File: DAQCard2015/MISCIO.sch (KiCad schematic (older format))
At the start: 3 parts

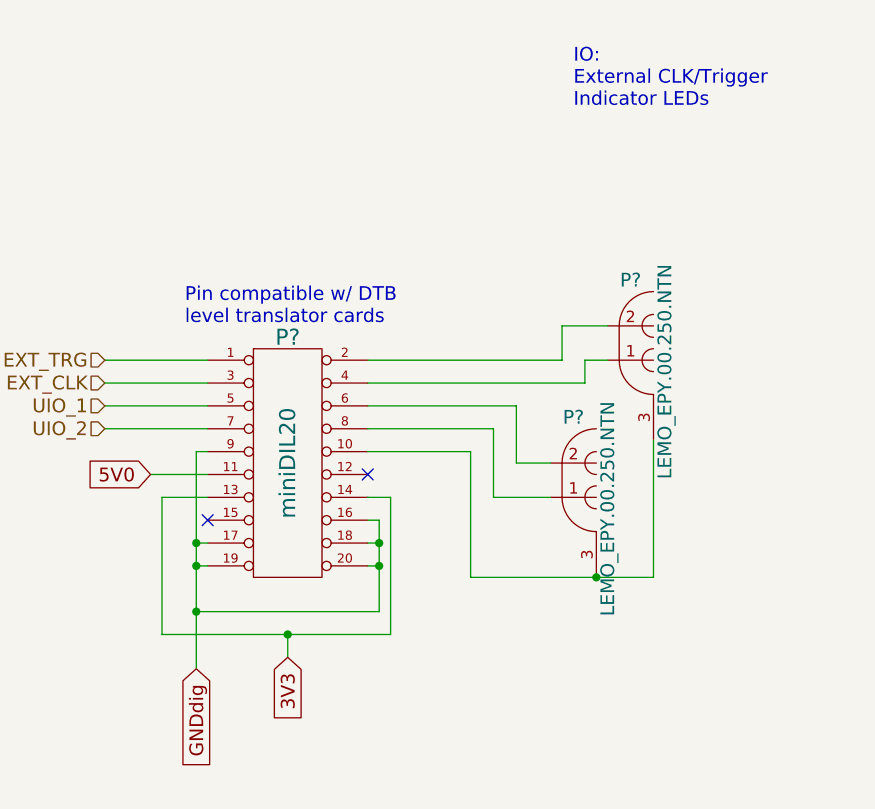
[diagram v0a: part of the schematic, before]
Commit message: Adds power circuitry to DAQCard2015
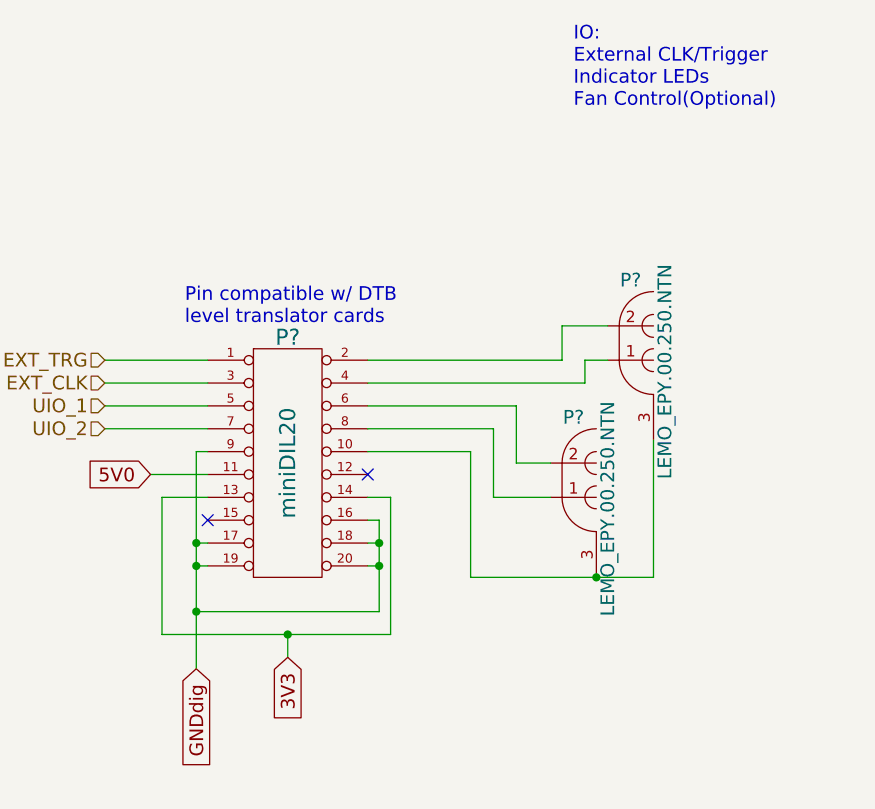
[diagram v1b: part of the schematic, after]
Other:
- note added: "IO:\nExternal CLK/Trigger\nIndicator LEDs\nFan Control(Optional)"
- note removed: "IO:\nExternal CLK/Trigger\nIndicator LEDs"
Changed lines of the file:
@@
 $EndDescr
 Text Notes 9050 900  0    60   ~ 0
-IO:\nExternal CLK/Trigger\nIndicator LEDs
+IO:\nExternal CLK/Trigger\nIndicator LEDs\nFan Control(Optional)
 $Comp
 L LEMO_EPY.00.250.NTN P?
@@
 $EndComp
 Wire Wire Line
-	7400 2400 7400 2800
-Wire Wire Line
-	7400 2800 7400 2900
-Wire Wire Line
-	7400 2900 7400 3100
-Wire Wire Line
-	7400 3100 7400 3350
+	7400 2400 7400 3350
 Wire Wire Line
 	8150 2700 8200 2700
 Wire Wire Line
-	8200 2700 8200 2800
-Wire Wire Line
-	8200 2800 8200 2900
-Wire Wire Line
-	8200 2900 8200 3100
+	8200 2700 8200 3100
 Wire Wire Line
 	8200 3100 7400 3100
@@
 	8150 2600 8250 2600
 Wire Wire Line
-	8250 2600 8250 3200
+	8250 3200 8250 2600
 Wire Wire Line
-	8250 3200 7800 3200
-Wire Wire Line
-	7800 3200 7250 3200
+	7250 3200 8250 3200
 Wire Wire Line
 	7250 3200 7250 2600
@@
 	8600 2400 8600 2950
 Wire Wire Line
-	8600 2950 9150 2950
-Wire Wire Line
-	9150 2950 9400 2950
+	8600 2950 9400 2950
 Wire Wire Line
 	9400 2950 9400 2350

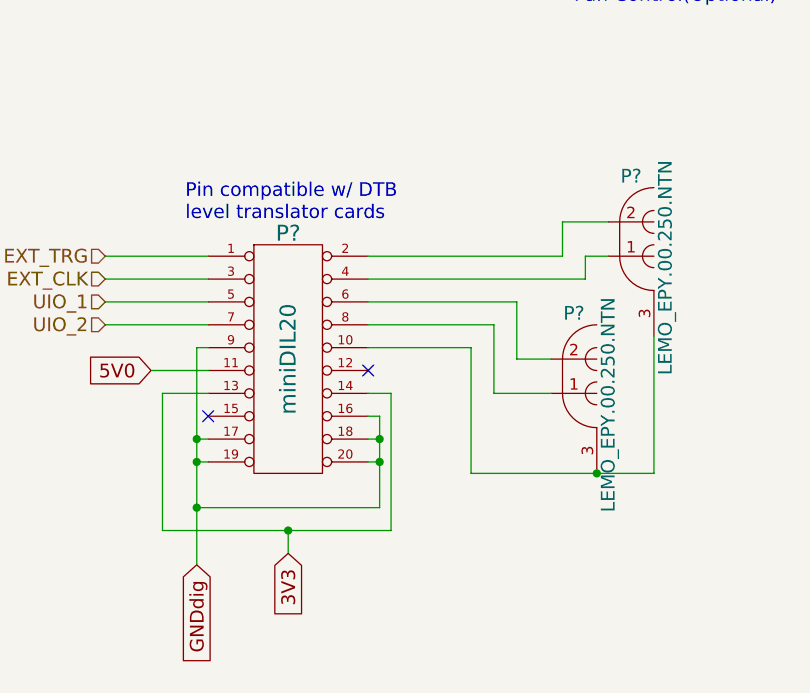
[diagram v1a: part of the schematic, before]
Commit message: Replaces single ample with 4-channel varients. Greatly reducing part count
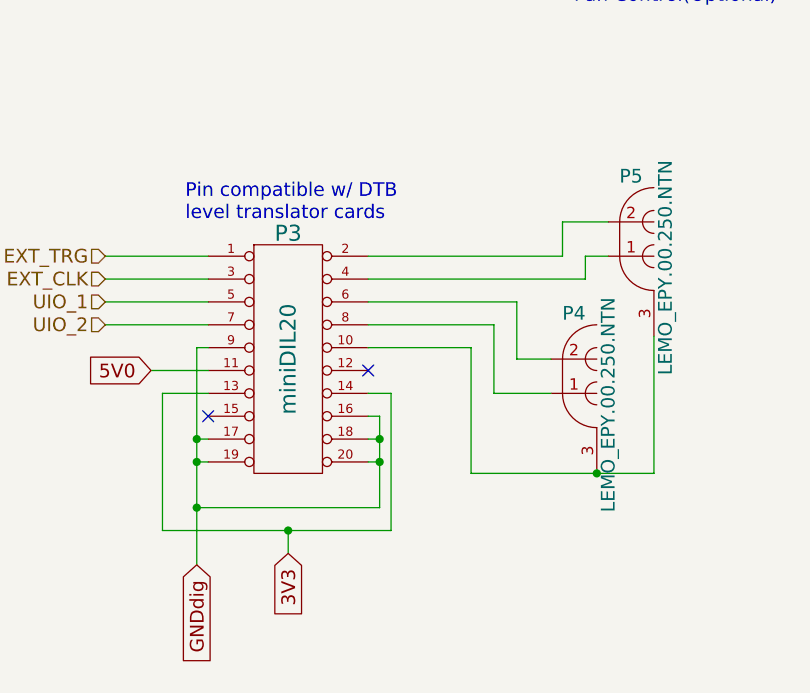
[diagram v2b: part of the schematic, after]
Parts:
- gave numbers to parts that had none: 3
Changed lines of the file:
@@
 IO:\nExternal CLK/Trigger\nIndicator LEDs\nFan Control(Optional)
 $Comp
-L LEMO_EPY.00.250.NTN P?
+L LEMO_EPY.00.250.NTN P5
 U 1 1 55D34F59
 P 9400 2000
-F 0 "P?" H 9300 2350 60  0000 C CNN
+F 0 "P5" H 9300 2350 60  0000 C CNN
 F 1 "LEMO_EPY.00.250.NTN" V 9450 1950 60  0000 C CNN
 F 2 "" H 9400 2000 60  0000 C CNN
@@
 $EndComp
 $Comp
-L LEMO_EPY.00.250.NTN P?
+L LEMO_EPY.00.250.NTN P4
 U 1 1 55D35009
 P 9150 2600
-F 0 "P?" H 9050 2950 60  0000 C CNN
+F 0 "P4" H 9050 2950 60  0000 C CNN
 F 1 "LEMO_EPY.00.250.NTN" V 9200 2550 60  0000 C CNN
 F 2 "" H 9150 2600 60  0000 C CNN
@@
 	8700 2300 8150 2300
 $Comp
-L miniDIL20 P?
+L miniDIL20 P3
 U 1 1 55D35BC1
 P 7800 2450
-F 0 "P?" H 7800 3000 70  0000 C CNN
+F 0 "P3" H 7800 3000 70  0000 C CNN
 F 1 "miniDIL20" V 7800 2450 70  0000 C CNN
 F 2 "" H 7800 2450 60  0000 C CNN
@@
 	8150 2600 8250 2600
 Wire Wire Line
-	8250 3200 8250 2600
+	8250 2600 8250 3200
 Wire Wire Line
-	7250 3200 8250 3200
+	8250 3200 7250 3200
 Wire Wire Line
 	7250 3200 7250 2600

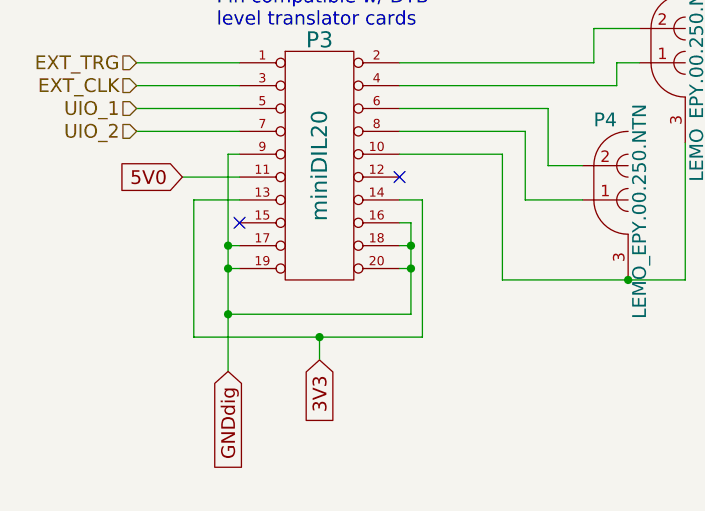
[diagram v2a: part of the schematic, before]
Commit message: Finishes initial version of schematic(mostly). And adds a whole bunch of new footprints!
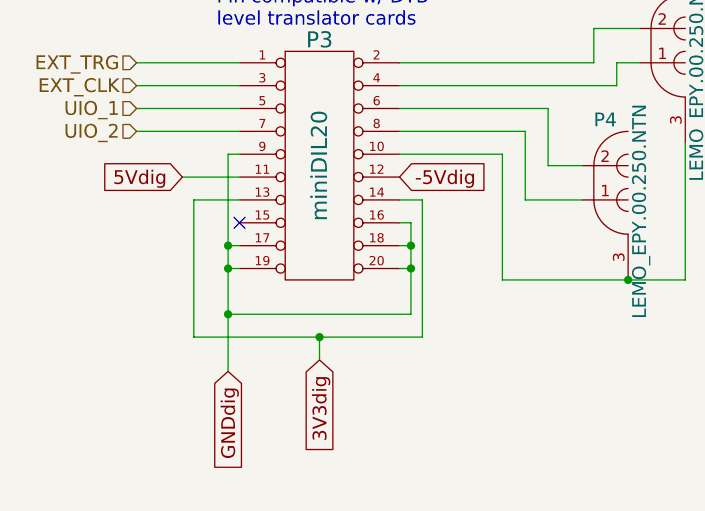
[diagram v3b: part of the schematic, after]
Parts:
- P3: footprint (none) -> extras:M50-3101045
- P4, P5: footprint (none) -> extras:EPY.00.250.NTN
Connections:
- net -5Vdig: now reaches P3.12
- net 3V3 renamed 3V3dig
- net 5V0 renamed 5Vdig
- no-connect marks 2 -> 1
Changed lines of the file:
@@
 F 0 "P5" H 9300 2350 60  0000 C CNN
 F 1 "LEMO_EPY.00.250.NTN" V 9450 1950 60  0000 C CNN
-F 2 "" H 9400 2000 60  0000 C CNN
+F 2 "extras:EPY.00.250.NTN" H 9400 2000 60  0001 C CNN
 F 3 "" H 9400 2000 60  0000 C CNN
 	1    9400 2000
@@
 F 0 "P4" H 9050 2950 60  0000 C CNN
 F 1 "LEMO_EPY.00.250.NTN" V 9200 2550 60  0000 C CNN
-F 2 "" H 9150 2600 60  0000 C CNN
+F 2 "extras:EPY.00.250.NTN" H 9150 2600 60  0001 C CNN
 F 3 "" H 9150 2600 60  0000 C CNN
 	1    9150 2600
@@
 	7400 2800 7450 2800
 NoConn ~ 7450 2700
-NoConn ~ 8150 2500
 Wire Wire Line
 	9200 1850 9000 1850
@@
 F 0 "P3" H 7800 3000 70  0000 C CNN
 F 1 "miniDIL20" V 7800 2450 70  0000 C CNN
-F 2 "" H 7800 2450 60  0000 C CNN
+F 2 "extras:M50-3101045" H 7800 2450 60  0001 C CNN
 F 3 "" H 7800 2450 60  0000 C CNN
 	1    7800 2450
@@
 $EndComp
 Text GLabel 7800 3300 3    60   Input ~ 0
-3V3
+3V3dig
 Wire Wire Line
 	8150 2600 8250 2600
@@
 	7250 2600 7450 2600
 Text GLabel 7200 2500 0    60   Input ~ 0
-5V0
+5Vdig
 Wire Wire Line
 	7450 2500 7200 2500
@@
 Text HLabel 7000 2300 0    60   Input ~ 0
 UIO_2
+Text GLabel 8150 2500 2    60   Input ~ 0
+-5Vdig
 $EndSCHEMATC

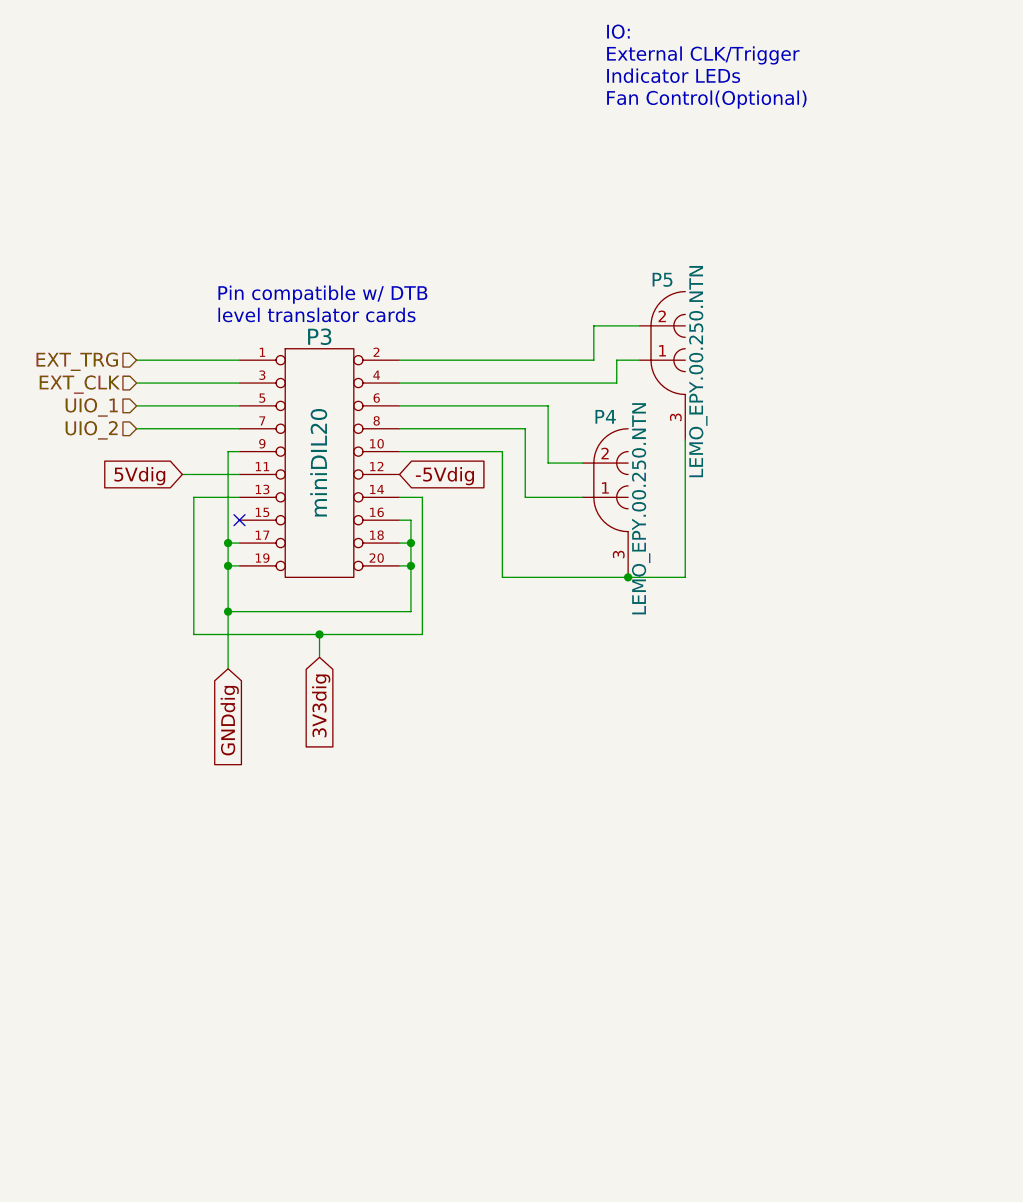
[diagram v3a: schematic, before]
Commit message: ADC channels wired, fan controller added
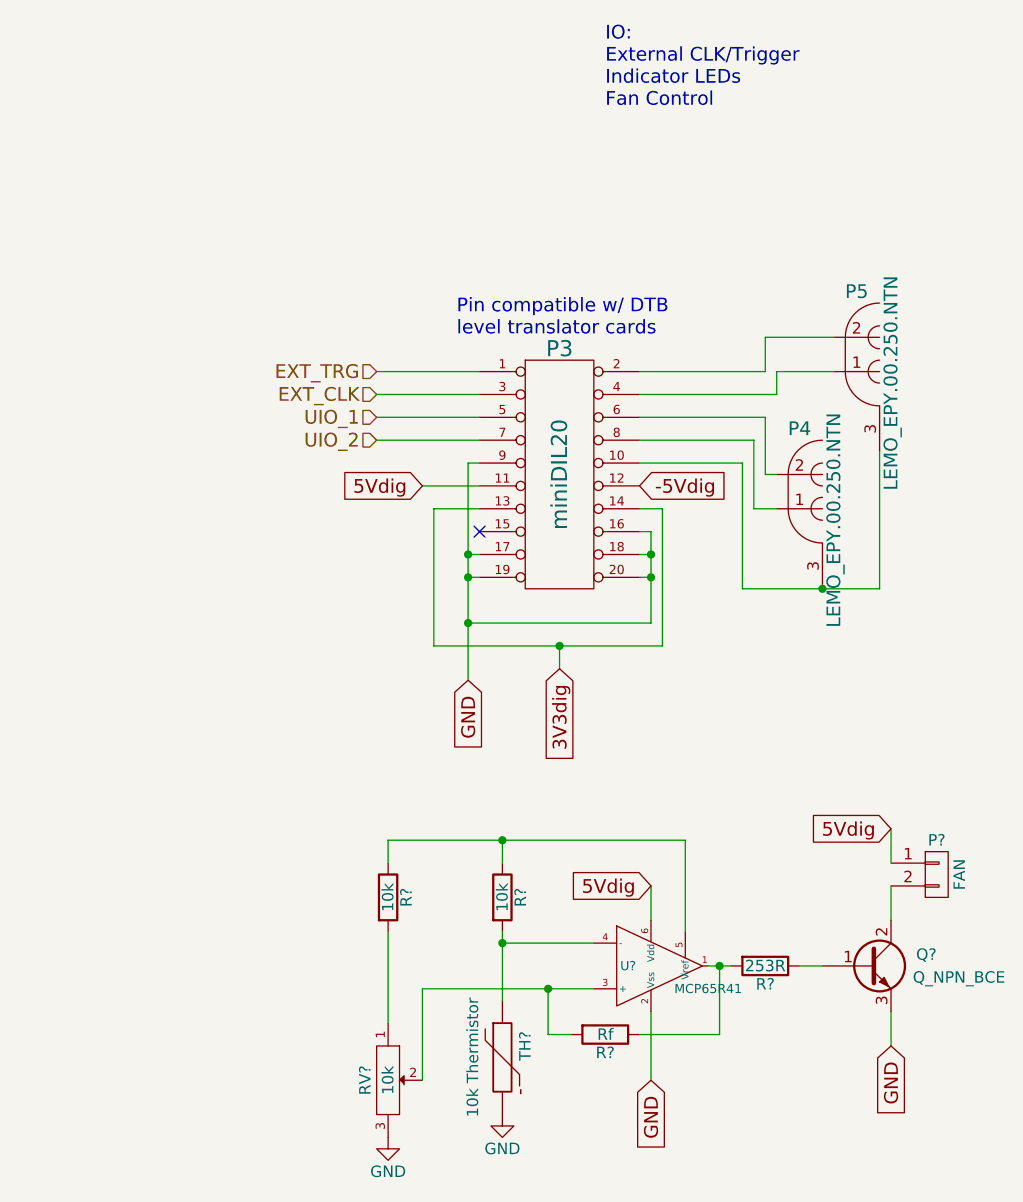
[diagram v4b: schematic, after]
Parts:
- added P?: FAN, symbol CONN_01X02
- added Q?: Q_NPN_BCE, symbol Q_NPN_BCE
- added R? (x2): 10k, symbol R
- added R?: 253R, symbol R
- added R?: Rf, symbol R
- added RV?: 10k, symbol POT
- added TH?: 10k Thermistor, symbol THERMISTOR
- added U?: MCP65R41, symbol MCP65R41
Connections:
- net 5Vdig: now also P?.1 (P1), U?.6 (Vdd)
- net GNDdig renamed GND
- net GND: now also Q?.3 (E), RV?.3, TH?.2, U?.2 (Vss)
- new net: R?.1, R?.1, U?.5 (Vref)
- new net: R?.2, RV?.1
- new net: R?.2, TH?.1, U?.4 (-)
- new net: R?.2, RV?.2, U?.3 (+)
- new net: R?.1, R?.2, U?.1
- new net: Q?.1 (B), R?.1
- new net: P?.2 (P2), Q?.2 (C)
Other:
- note added: "IO:\nExternal CLK/Trigger\nIndicator LEDs\nFan Control"
- note removed: "IO:\nExternal CLK/Trigger\nIndicator LEDs\nFan Control(Optional)"
- moved on the sheet: P3, P4, P5

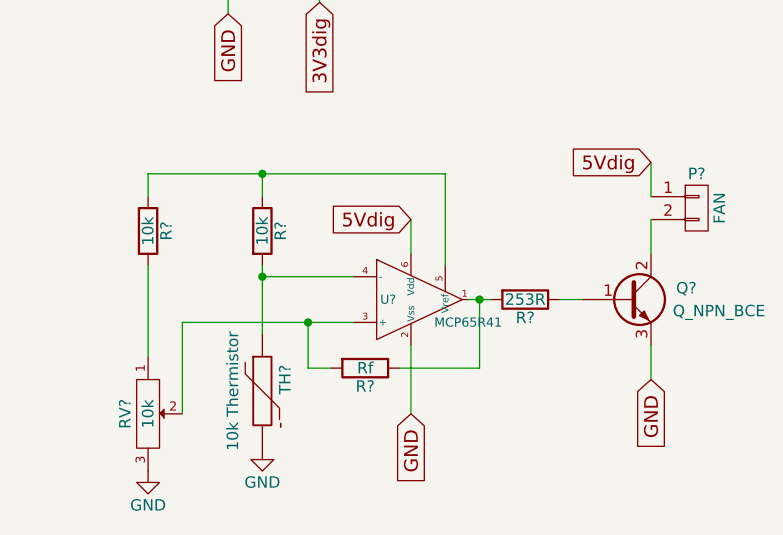
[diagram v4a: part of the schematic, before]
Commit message: Set proper hysterisis feedback in fan control
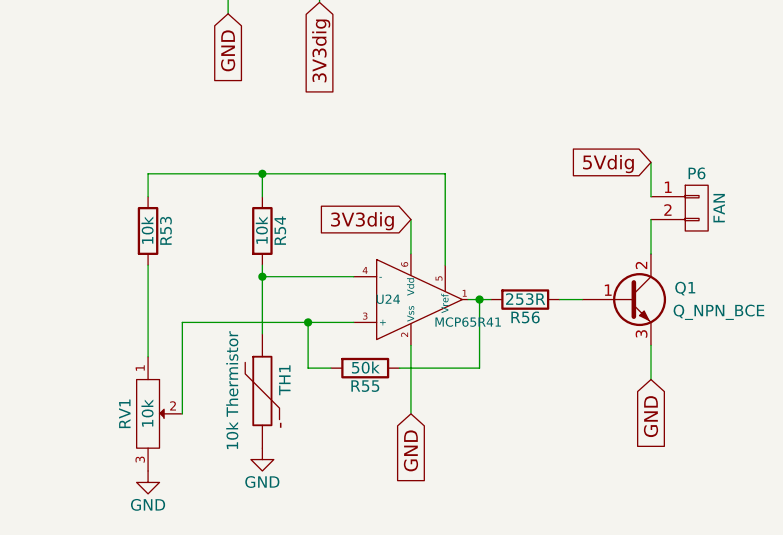
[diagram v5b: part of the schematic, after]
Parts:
- R55: renamed from R?; value Rf -> 50k
- gave numbers to parts that had none: 8
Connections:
- net 3V3dig: now also U24.6 (Vdd)
- net 5Vdig: no longer U24.6 (Vdd)
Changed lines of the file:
@@
 -5Vdig
 $Comp
-L R R?
+L R R53
 U 1 1 55F01621
 P 8100 4350
-F 0 "R?" V 8180 4350 50  0000 C CNN
+F 0 "R53" V 8180 4350 50  0000 C CNN
 F 1 "10k" V 8100 4350 50  0000 C CNN
 F 2 "" V 8030 4350 30  0000 C CNN
@@
 $EndComp
 $Comp
-L R R?
+L R R54
 U 1 1 55F016DC
 P 8600 4350
-F 0 "R?" V 8680 4350 50  0000 C CNN
+F 0 "R54" V 8680 4350 50  0000 C CNN
 F 1 "10k" V 8600 4350 50  0000 C CNN
 F 2 "" V 8530 4350 30  0000 C CNN
@@
 $EndComp
 $Comp
-L POT RV?
+L POT RV1
 U 1 1 55F0172C
 P 8100 5150
-F 0 "RV?" H 8100 5050 50  0000 C CNN
+F 0 "RV1" H 8100 5050 50  0000 C CNN
 F 1 "10k" H 8100 5150 50  0000 C CNN
 F 2 "" H 8100 5150 60  0000 C CNN
@@
 $EndComp
 $Comp
-L MCP65R41 U?
+L MCP65R41 U24
 U 1 1 55F01A3A
 P 9100 4650
-F 0 "U?" H 9150 4650 40  0000 C CNN
+F 0 "U24" H 9150 4650 40  0000 C CNN
 F 1 "MCP65R41" H 9500 4550 40  0000 C CNN
 F 2 "" H 9100 4650 60  0000 C CNN
@@
 	9250 4850 9250 5150
 Text GLabel 9250 4300 0    60   Input ~ 0
-5Vdig
+3V3dig
 Text GLabel 9250 5150 3    60   Input ~ 0
 GND
 $Comp
-L THERMISTOR TH?
+L THERMISTOR TH1
 U 1 1 55F02184
 P 8600 5050
-F 0 "TH?" V 8700 5100 50  0000 C CNN
+F 0 "TH1" V 8700 5100 50  0000 C CNN
 F 1 "10k Thermistor" V 8500 5050 50  0000 C BNN
 F 2 "" H 8600 5050 60  0000 C CNN
@@
 	8600 4500 8600 4800
 $Comp
-L GND #PWR?
+L GND #PWR1
 U 1 1 55F022ED
 P 8100 5400
-F 0 "#PWR?" H 8100 5150 50  0001 C CNN
+F 0 "#PWR1" H 8100 5150 50  0001 C CNN
 F 1 "GND" H 8100 5250 50  0000 C CNN
 F 2 "" H 8100 5400 60  0000 C CNN
@@
 $EndComp
 $Comp
-L GND #PWR?
+L GND #PWR2
 U 1 1 55F02317
 P 8600 5300
-F 0 "#PWR?" H 8600 5050 50  0001 C CNN
+F 0 "#PWR2" H 8600 5050 50  0001 C CNN
 F 1 "GND" H 8600 5150 50  0000 C CNN
 F 2 "" H 8600 5300 60  0000 C CNN
@@
 	8100 4100 9400 4100
 $Comp
-L Q_NPN_BCE Q?
+L Q_NPN_BCE Q1
 U 1 1 55F036FA
 P 10200 4650
-F 0 "Q?" H 10500 4700 50  0000 R CNN
+F 0 "Q1" H 10500 4700 50  0000 R CNN
 F 1 "Q_NPN_BCE" H 10800 4600 50  0000 R CNN
 F 2 "" H 10400 4750 29  0000 C CNN
@@
 $EndComp
 $Comp
-L R R?
+L R R56
 U 1 1 55F03778
 P 9750 4650
-F 0 "R?" V 9830 4650 50  0000 C CNN
+F 0 "R56" V 9830 4650 50  0000 C CNN
 F 1 "253R" V 9750 4650 50  0000 C CNN
 F 2 "" V 9680 4650 30  0000 C CNN
@@
 	9900 4650 10000 4650
 $Comp
-L CONN_01X02 P?
+L CONN_01X02 P6
 U 1 1 55F03A28
 P 10500 4250
-F 0 "P?" H 10500 4400 50  0000 C CNN
+F 0 "P6" H 10500 4400 50  0000 C CNN
 F 1 "FAN" V 10600 4250 50  0000 C CNN
 F 2 "" H 10500 4250 60  0000 C CNN
@@
 GND
 $Comp
-L R R?
+L R R55
 U 1 1 55F04DE6
 P 9050 4950
-F 0 "R?" V 9130 4950 50  0000 C CNN
-F 1 "Rf" V 9050 4950 50  0000 C CNN
+F 0 "R55" V 9130 4950 50  0000 C CNN
+F 1 "50k" V 9050 4950 50  0000 C CNN
 F 2 "" V 8980 4950 30  0000 C CNN
 F 3 "" H 9050 4950 30  0000 C CNN
